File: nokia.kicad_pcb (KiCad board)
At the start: 2 copper layers, 42.1 x 108 mm, 21 parts, among them J1 Conn_01x07, J3 Conn_01x04_Pin, J4 Conn_01x04, M1 Motor_DC, SW1 SW_Push, U1 Pico

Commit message: 2nd iteration of board
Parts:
- added C10: 4.7u, Capacitor_SMD:C_0402_1005Metric, B.Cu at (35.0, 59.8)
- added C11: 100n, Capacitor_SMD:C_0402_1005Metric, B.Cu at (43.2, 53.5)
- added C12: 100n, Capacitor_SMD:C_0402_1005Metric, B.Cu at (49.0, 59.8)
- added C13: 100n, Capacitor_SMD:C_0402_1005Metric, B.Cu at (35.6, 62.0)
- added C14: 100n, Capacitor_SMD:C_0402_1005Metric, B.Cu at (49.9, 63.2)
- added C15: 100n, Capacitor_SMD:C_0402_1005Metric, B.Cu at (45.6, 67.8)
- added C16: 100n, Capacitor_SMD:C_0402_1005Metric, B.Cu at (42.2, 53.4)
- added C17: 100n, Capacitor_SMD:C_0402_1005Metric, B.Cu at (40.5, 66.9)
- added C18: 100n, Capacitor_SMD:C_0402_1005Metric, B.Cu at (38.4, 53.6)
- added C19: 10u, Capacitor_SMD:C_0805_2012Metric, B.Cu at (36.1, 114.0)
- added C2: 100n, Capacitor_SMD:C_0402_1005Metric, F.Cu at (112.0, 110.4)
- added C20: 100n, Capacitor_SMD:C_0402_1005Metric, B.Cu at (46.8, 53.6)
- added C21: 100n, Capacitor_SMD:C_0402_1005Metric, B.Cu at (35.7, 63.4)
- added C3: 15p, Capacitor_SMD:C_0402_1005Metric, B.Cu at (27.8, 63.2)
- added C4: 15p, Capacitor_SMD:C_0402_1005Metric, B.Cu at (27.8, 62.2)
- added C5: 10u, Capacitor_SMD:C_0805_2012Metric, B.Cu at (44.9, 72.5)
- added C6: 4.7u, Capacitor_SMD:C_0402_1005Metric, B.Cu at (48.6, 57.2)
- added C7: 4.7u, Capacitor_SMD:C_0402_1005Metric, B.Cu at (49.6, 57.2)
- added C79: 100nF, Capacitor_SMD:C_0402_1005Metric, B.Cu at (35.2, 37.0)
- added C8: 100n, Capacitor_SMD:C_0402_1005Metric, B.Cu at (42.6, 67.1)
- added C9: 4.7u, Capacitor_SMD:C_0402_1005Metric, B.Cu at (49.1, 55.0)
- added J2: USB_B_Micro, Connector_USB:USB_Micro-B_Amphenol_10103594-0001LF_Horizontal, B.Cu at (50.4, 124.2)
- added J20: Conn_01x04_Pin, Battery:battery, B.Cu at (39.0, 45.1)
- added J5: Conn_02x06_Top_Bottom, Connector_PinHeader_2.54mm:PinHeader_2x06_P2.54mm_Vertical_SMD, B.Cu at (43.9, 32.3)
- added J6: SM03B-SRSS-TB, Connector_JST:JST_SH_SM03B-SRSS-TB_1x03-1MP_P1.00mm_Horizontal, B.Cu at (33.2, 122.8)
- added JP17: SolderJumper_2_Open, Jumper:SolderJumper-2_P1.3mm_Open_RoundedPad1.0x1.5mm, B.Cu at (36.0, 39.5)
- added KPDOWN1: Jumper_2_Open, Jumper:ButtonPads, F.Cu at (50.0, 90.0)
- added KPSELECT1: Jumper_2_Open, Jumper:ButtonPads, F.Cu at (43.0, 82.2)
- added KPUP1: Jumper_2_Open, Jumper:ButtonPads, F.Cu at (56.8, 84.8)
- added R1: DNF, Resistor_SMD:R_0402_1005Metric, F.Cu at (109.1, 110.4)
- added R10: 0, Resistor_SMD:R_0402_1005Metric, F.Cu at (109.1, 114.4)
- added R2: 1k, Resistor_SMD:R_0402_1005Metric, B.Cu at (33.2, 60.8)
- added R3: 33, Resistor_SMD:R_0402_1005Metric, B.Cu at (51.0, 55.0)
- added R6: 1k, Resistor_SMD:R_0402_1005Metric, B.Cu at (31.0, 21.4)
- added R7: 27, Resistor_SMD:R_0402_1005Metric, B.Cu at (51.1, 59.2)
- added R8: 27, Resistor_SMD:R_0402_1005Metric, B.Cu at (51.1, 58.2)
- added R9: DNF, Resistor_SMD:R_0402_1005Metric, F.Cu at (109.1, 112.4)
- added U4: NCP1117-3.3_SOT223, Package_TO_SOT_SMD:SOT-223-3_TabPin2, B.Cu at (50.3, 74.4)
- added U5: RP2350_80QFN, RP2350_80QFN_minimal:RP2350-QFN-80-1EP_10x10_P0.4mm_EP3.4x3.4mm_ThermalVias, B.Cu at (42.5, 60.2)
- added Y1: ABM8-272-T3, Crystal:Crystal_SMD_3225-4Pin_3.2x2.5mm, B.Cu at (30.4, 61.6)
- C1: value C -> 10u
- J3: value Conn_01x04_Pin -> SM03B-SRSS-TB; footprint Battery:battery -> Connector_JST:JST_SH_SM03B-SRSS-TB_1x03-1MP_P1.00mm_Horizontal
- J4: value Conn_01x04 -> Conn_01x06_Pin; footprint Connector_PinHeader_2.54mm:PinHeader_1x04_P2.54mm_Vertical -> Connector:sim connector connector; moved to B.Cu
- U1: value Pico -> W25Q128JVS; footprint MCU_RaspberryPi_and_Boards:RPi_Pico_SMD_TH -> Package_SO:SOIC-8_5.23x5.23mm_P1.27mm; moved to F.Cu
- moved J3 77.7 mm to (40.2, 122.8)
- moved J4 75.9 mm to (43.7, 121.9), turned to 180 degrees
- moved U1 72.3 mm to (112.8, 106.0)
- moved C1 45.7 mm to (55.7, 74.2), turned to 90 degrees
- moved J1 0.50 mm to (42.7, 45.7)
- renumbered JP12 to KP#1, JP10 to KP*1, JP11 to KP0, JP1 to KP1, JP2 to KP2, JP3 to KP3, JP4 to KP4, JP5 to KP5, JP6 to KP6, JP7 to KP7, JP8 to KP8, JP9 to KP9, JP13 to KPC1
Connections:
- C1 pad 1: Net-(J1-Pin_7) -> VBUS
- C1 pad 2: Net-(J1-Pin_5) -> GND
- J1 pad 2: Net-(J1-Pin_2) -> /GPIO38
- J1 pad 3: Net-(J1-Pin_3) -> /GPIO39
- J1 pad 4: Net-(J1-Pin_4) -> /GPIO36
- J1 pad 5: Net-(J1-Pin_5) -> /GPIO37
- J1 pad 8: Net-(J1-Pin_8) -> /GPIO33
- J3 pad 1: Net-(J3-Pin_1) -> /GPIO1
- J3 pad 2: Net-(J3-Pin_2) -> GND
- J3 pad 3: Net-(J3-Pin_3) -> /GPIO0
- J4 pad 1: Net-(J3-Pin_1) -> +3V3
- J4 pad 2: Net-(J3-Pin_2) -> /GPIO23
- J4 pad 3: Net-(J3-Pin_3) -> /GPIO15
- KP#1 pad 1: Net-(JP12-A) -> +3V3
- KP#1 pad 2: +3V3 -> /GPIO4
- KP*1 pad 1: Net-(JP10-A) -> +3V3
- KP*1 pad 2: +3V3 -> /GPIO20
- KP0 pad 2: Net-(JP11-B) -> /GPIO10
- KP1 pad 1: Net-(JP1-A) -> +3V3
- KP1 pad 2: +3V3 -> /GPIO17
- KP2 pad 1: Net-(JP2-A) -> +3V3
- KP2 pad 2: +3V3 -> /GPIO13
- KP3 pad 1: Net-(JP3-A) -> +3V3
- KP3 pad 2: +3V3 -> /GPIO7
- KP4 pad 1: Net-(JP4-A) -> +3V3
- KP4 pad 2: +3V3 -> /GPIO18
- KP5 pad 2: Net-(JP5-B) -> /GPIO14
- KP6 pad 1: Net-(JP6-A) -> +3V3
- KP6 pad 2: +3V3 -> /GPIO6
- KP7 pad 1: Net-(JP7-A) -> +3V3
- KP7 pad 2: +3V3 -> /GPIO19
- KP8 pad 1: Net-(JP8-A) -> +3V3
- KP8 pad 2: +3V3 -> /GPIO11
- KP9 pad 1: Net-(JP9-A) -> +3V3
- KP9 pad 2: +3V3 -> /GPIO5
- KPC1 pad 2: Net-(JP13-B) -> /GPIO16
- LS2 pad 1: Net-(U1-GPIO4) -> /GPIO21
- LS2 pad 2: Net-(LS2-Pad2) -> GND
- M1 pad 1: Net-(M1-+) -> /GPIO2
- M1 pad 2: Net-(M1--) -> GND
- SW1 pad 1: GND -> Net-(R6-Pad1)
- SW1 pad 2: Net-(U1-RUN) -> /RUN
- U1 pad 1: Net-(JP10-A) -> /FLASH_SS
- U1 pad 2: Net-(JP11-B) -> /QSPI_SD1
- U1 pad 3: Net-(LS2-Pad2) -> /QSPI_SD2
- U1 pad 4: Net-(JP7-A) -> GND
- U1 pad 5: Net-(JP8-A) -> /QSPI_SD0
- U1 pad 6: Net-(U1-GPIO4) -> /QSPI_SCLK
- U1 pad 7: Net-(JP5-B) -> /QSPI_SD3
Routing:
- net +3V3: track 159.9 -> 26.1 mm, vias 15 -> 20
- net Net-(U1-RUN): track 91.8 -> 0.00 mm
- net /GPIO0: track 0.00 -> 90.0 mm, vias 0 -> 2
- net /GPIO1: track 0.00 -> 87.1 mm, vias 0 -> 2
- net /SWD: track 0.00 -> 82.3 mm, vias 0 -> 2
- net /SWCLK: track 0.00 -> 82.2 mm, vias 0 -> 2
- net /USB_D-: track 0.00 -> 78.0 mm
- net Net-(J1-Pin_5): track 77.9 -> 0.00 mm, vias 1 -> 0
- net /USB_D+: track 0.00 -> 76.6 mm
- net /GPIO20: track 0.00 -> 68.6 mm, vias 0 -> 2
- net /GPIO4: track 0.00 -> 68.4 mm, vias 0 -> 2
- net /GPIO19: track 0.00 -> 60.2 mm, vias 0 -> 2
- net /GPIO5: track 0.00 -> 60.1 mm, vias 0 -> 2
- net /GPIO18: track 0.00 -> 56.4 mm, vias 0 -> 2
- net /GPIO6: track 0.00 -> 56.2 mm, vias 0 -> 2
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- added copper zone on In1.Cu, net +3V3
- added copper zone on B.Cu, net GND
- added copper zone on F.Cu, net GND
- added copper zone on In2.Cu, net GND
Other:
- outline, holes or cut-outs redrawn
- copper layers 2 -> 4

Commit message: 2nd iteration of board
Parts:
- removed J5: Conn_02x06_Top_Bottom, Connector_PinHeader_2.54mm:PinHeader_2x06_P2.54mm_Vertical_SMD
- added D1: D, Diode_SMD:D_0402_1005Metric, B.Cu at (57.2, 99.2)
- added D2: LED_ARGB, LED_SMD:RGBLED-reverse, B.Cu at (28.1, 77.9)
- added D3: LED_ARGB, LED_SMD:RGBLED-reverse, B.Cu at (51.5, 115.9)
- added D4: LED_ARGB, LED_SMD:RGBLED-reverse, B.Cu at (57.6, 77.9)
- added D5: LED_ARGB, LED_SMD:RGBLED-reverse, B.Cu at (34.0, 115.9)
- added D6: LED_ARGB, LED_SMD:RGBLED-reverse, B.Cu at (47.4, 77.9)
- added D7: LED_ARGB, LED_SMD:RGBLED-reverse, B.Cu at (51.5, 101.0)
- added D8: LED_ARGB, LED_SMD:RGBLED-reverse, B.Cu at (38.2, 77.9)
- added D9: LED_ARGB, LED_SMD:RGBLED-reverse, B.Cu at (34.0, 101.0)
- added Q1: BC847, Package_TO_SOT_SMD:SOT-23, B.Cu at (58.2, 101.5)
- added R11: 90, Resistor_SMD:R_0402_1005Metric, B.Cu at (54.4, 99.2)
- added R12: 90, Resistor_SMD:R_0402_1005Metric, B.Cu at (49.8, 100.7)
- added R13: 140, Resistor_SMD:R_0402_1005Metric, B.Cu at (36.8, 98.2)
- added R14: 90, Resistor_SMD:R_0402_1005Metric, B.Cu at (36.7, 99.2)
- added R15: 90, Resistor_SMD:R_0402_1005Metric, B.Cu at (30.6, 99.0)
- added R16: 90, Resistor_SMD:R_0402_1005Metric, B.Cu at (50.3, 75.8)
- added R17: 90, Resistor_SMD:R_0402_1005Metric, B.Cu at (44.0, 76.0)
- added R18: 140, Resistor_SMD:R_0402_1005Metric, B.Cu at (40.9, 74.9)
- added R19: 90, Resistor_SMD:R_0402_1005Metric, B.Cu at (40.9, 76.0)
- added R20: 90, Resistor_SMD:R_0402_1005Metric, B.Cu at (34.9, 75.9)
- added R21: 140, Resistor_SMD:R_0402_1005Metric, B.Cu at (30.8, 74.8)
- added R22: 90, Resistor_SMD:R_0402_1005Metric, B.Cu at (30.8, 75.9)
- added R23: 90, Resistor_SMD:R_0402_1005Metric, B.Cu at (26.2, 77.5)
- added R24: 140, Resistor_SMD:R_0402_1005Metric, B.Cu at (54.3, 113.0)
- added R25: 90, Resistor_SMD:R_0402_1005Metric, B.Cu at (54.4, 114.0)
- added R26: 90, Resistor_SMD:R_0402_1005Metric, B.Cu at (49.8, 115.4)
- added R27: 140, Resistor_SMD:R_0402_1005Metric, B.Cu at (58.7, 73.2)
- added R28: 90, Resistor_SMD:R_0402_1005Metric, B.Cu at (58.8, 77.5)
- added R29: 90, Resistor_SMD:R_0402_1005Metric, B.Cu at (54.4, 75.9)
- added R30: 140, Resistor_SMD:R_0402_1005Metric, B.Cu at (36.9, 113.0)
- added R31: 90, Resistor_SMD:R_0402_1005Metric, B.Cu at (36.8, 114.0)
- added R32: 90, Resistor_SMD:R_0402_1005Metric, B.Cu at (30.7, 114.1)
- added R4: 140, Resistor_SMD:R_0402_1005Metric, B.Cu at (54.3, 97.9)
- added R5: 140, Resistor_SMD:R_0402_1005Metric, B.Cu at (50.3, 74.5)
- C2, R1, R10, R9, U1: moved to B.Cu
- LS2: value Speaker_Crystal -> Buzzer
- M1: value Motor_DC -> Vibration
- moved C2 76.9 mm to (53.7, 60.2)
- moved R9 75.4 mm to (51.5, 63.7), turned to -90 degrees
- moved R10 72.9 mm to (60.4, 60.0)
- moved R1 72.4 mm to (56.9, 60.1)
- moved U1 70.2 mm to (56.8, 63.6), turned to 180 degrees
- moved C1 19.3 mm to (45.4, 90.5), turned to -90 degrees
- moved C5 14.1 mm to (36.6, 83.9)
- moved U4 13.4 mm to (42.1, 85.0)
- moved C19 9.55 mm to (36.3, 104.5)
- moved C14 0.81 mm to (49.8, 64.0)
- moved C11 0.76 mm to (43.3, 52.8)
- moved C15 0.74 mm to (46.2, 68.2)
- moved C17 0.73 mm to (40.5, 67.7)
- moved C16 0.64 mm to (42.2, 52.8)
- moved C13 0.29 mm to (35.5, 61.7)
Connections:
- M1 pad 1: /GPIO2 -> +3V3
- M1 pad 2: GND -> Net-(D1-A)
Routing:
- net /GPIO34: track 0.00 -> 202.9 mm, vias 0 -> 9
- net /GPIO32: track 0.00 -> 177.8 mm, vias 0 -> 8
- net /GPIO30: track 0.00 -> 155.7 mm, vias 0 -> 9
- net /GPIO2: track 0.00 -> 48.3 mm, vias 0 -> 2
- net +3V3: track 26.1 -> 67.6 mm, vias 20 -> 41
- net /FLASH_SS: track 0.00 -> 22.9 mm
- net /QSPI_SD2: track 0.00 -> 19.1 mm, vias 0 -> 2
- net /GPIO39: track 32.0 -> 15.7 mm, vias 3 -> 2
- net VBUS: track 54.8 -> 39.0 mm
- net /QSPI_SCLK: track 0.00 -> 15.7 mm, vias 0 -> 2
- net /QSPI_SS: track 0.00 -> 14.4 mm, vias 0 -> 2
- net Net-(J1-Pin_7): track 17.4 -> 3.62 mm
- net /QSPI_SD1: track 0.00 -> 13.6 mm, vias 0 -> 2
- net GND: track 40.2 -> 52.2 mm, vias 28 -> 32
- net /QSPI_SD0: track 0.00 -> 11.4 mm, vias 0 -> 2
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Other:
- outline, holes or cut-outs redrawn

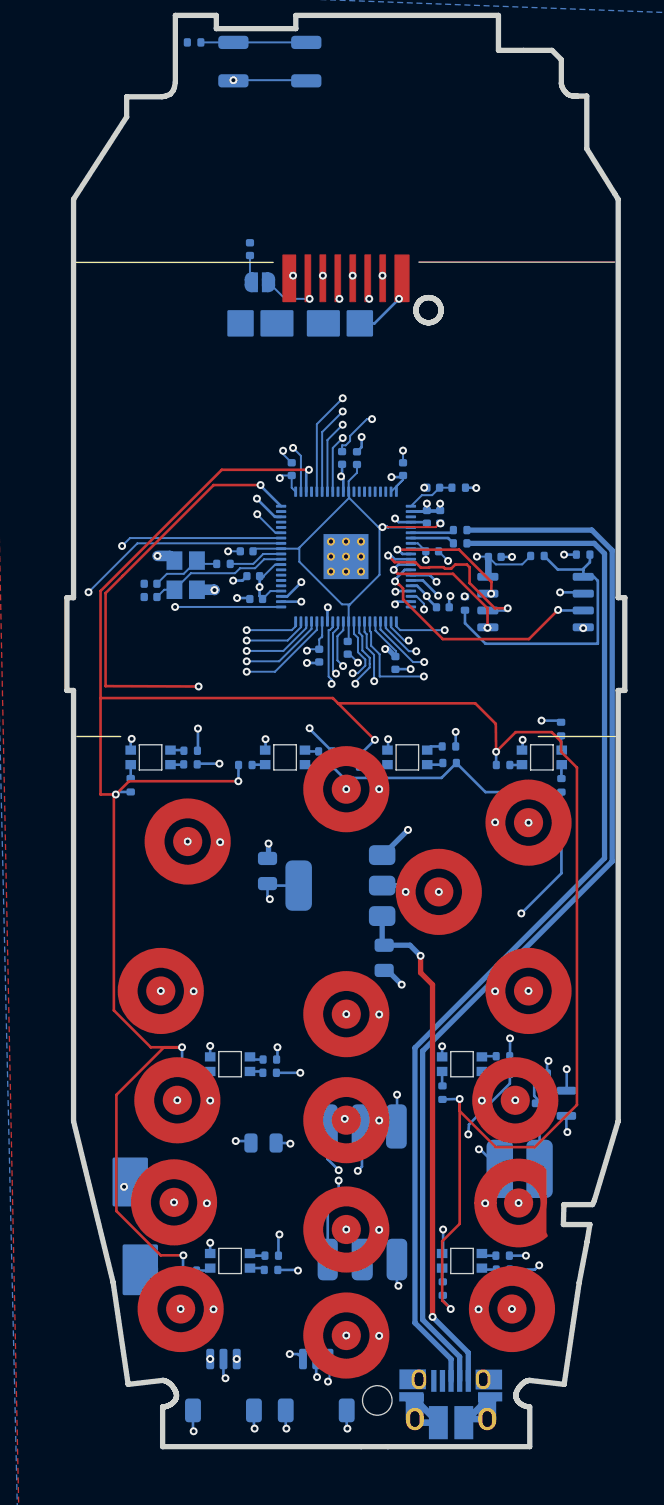
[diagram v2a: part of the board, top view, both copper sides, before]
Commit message: add breakout connector
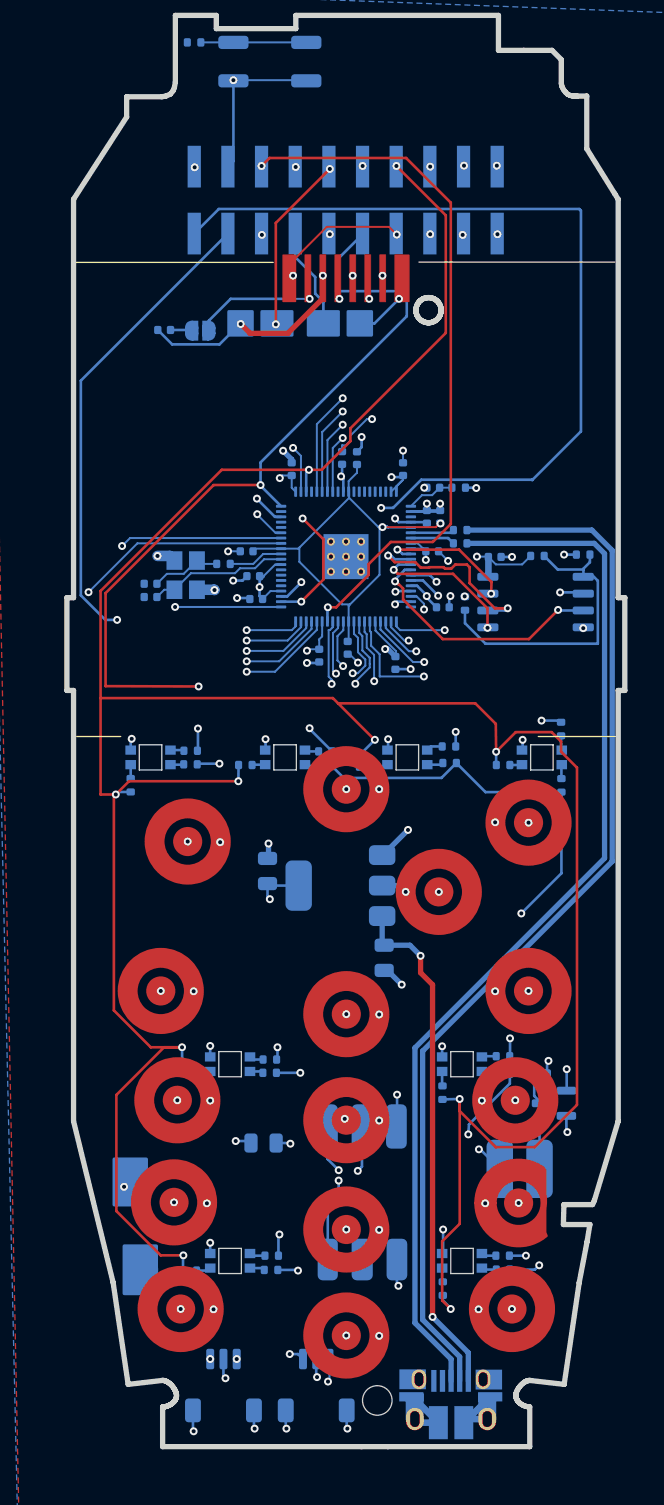
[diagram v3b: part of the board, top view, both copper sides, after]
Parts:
- added J5: Conn_02x10_Top_Bottom, Connector_PinHeader_2.54mm:PinHeader_2x10_P2.54mm_Vertical_SMD, B.Cu at (42.5, 33.3)
- moved C79 8.90 mm to (28.8, 43.1), turned to 0 degrees
- moved JP17 5.79 mm to (31.5, 43.1)
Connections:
- J20 pad 2: unconnected-(J20-Pin_2-Pad2) -> Net-(J20-Pin_2)
- J20 pad 3: unconnected-(J20-Pin_3-Pad3) -> Net-(J20-Pin_3)
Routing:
- net /GPIO2: track 48.3 -> 120.4 mm, vias 2 -> 3
- net /GPIO15: track 47.8 -> 100.3 mm, vias 2 -> 3
- net /GPIO23: track 52.7 -> 103.6 mm, vias 2 -> 3
- net /GPIO21: track 55.3 -> 102.7 mm, vias 2 -> 3
- net /GPIO22: track 53.4 -> 83.7 mm, vias 2 -> 4
- net /GPIO32: track 177.8 -> 206.7 mm
- net /GPIO34: track 202.9 -> 231.8 mm, vias 9 -> 10
- net /GPIO30: track 155.7 -> 183.9 mm, vias 9 -> 10
- net Net-(J20-Pin_3): track 0.00 -> 13.4 mm, vias 0 -> 2
- net GND: track 52.2 -> 65.2 mm, vias 32 -> 35
- net /GPIO39: track 15.7 -> 28.7 mm, vias 2 -> 3
- net /GPIO37: track 18.2 -> 29.3 mm, vias 2 -> 3
- net /GPIO33: track 19.5 -> 28.4 mm, vias 2 -> 3
- net Net-(J20-Pin_2): track 0.00 -> 7.65 mm
- net /GPIO38: track 18.0 -> 25.3 mm, vias 2 -> 3
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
